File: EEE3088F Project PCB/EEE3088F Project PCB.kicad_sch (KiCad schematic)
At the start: 53 parts, among them IC1 74LVC1G04SE-7, J1 JST PH 2.00mm connector, J3 TYPE-C-31-M-12, J4 TYPE-C-31-M-12, SW1 SS12D07VG5 087, U1 DRV8833PWR, U10 LM7805_TO220, U11 TC4056A., U2 DRV8833PWPR, U3 INA219AxD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

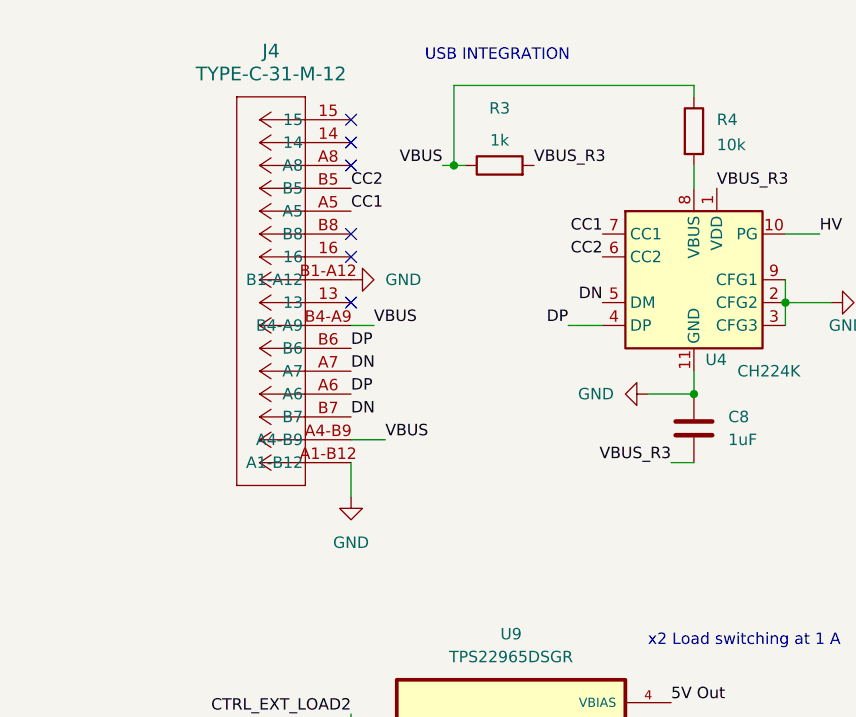
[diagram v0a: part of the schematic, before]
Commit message: Added student numbers, corrected board boundries, placed connectors (USB, JST, & pin headers)
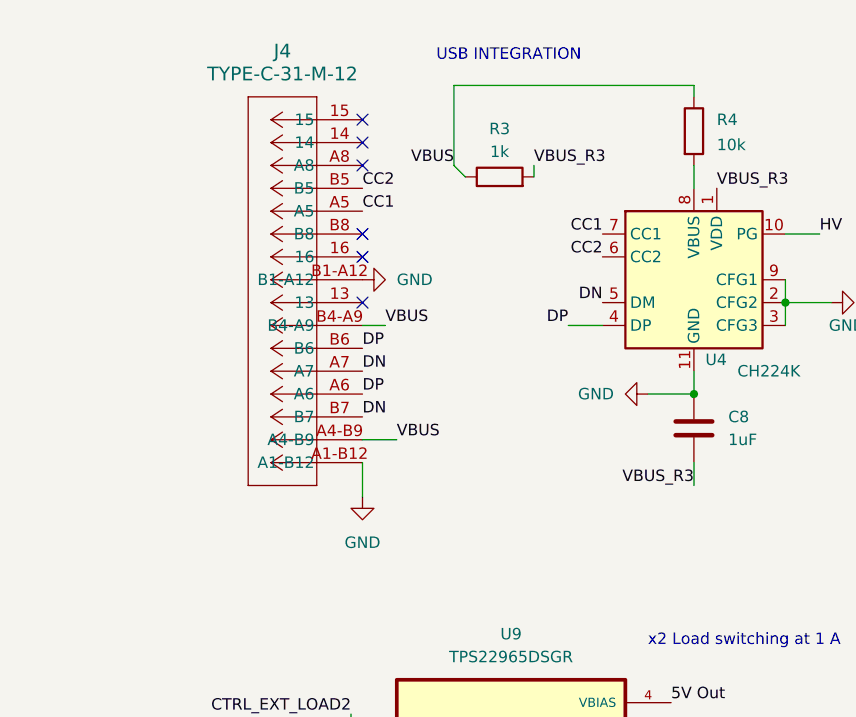
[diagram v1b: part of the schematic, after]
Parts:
- J3, J4: footprint CONN12_C-31-M-12_HRO -> (none)
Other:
- moved on the sheet: J4, R3
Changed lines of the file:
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@@
 	(text "USB INTEGRATION"
 		(exclude_from_sim no)
-		(at 48.006 15.748 0)
+		(at 49.276 15.748 0)
 		(effects
 			(font
@@
 	)
 	(junction
-		(at 43.18 27.94)
-		(diameter 0)
-		(color 0 0 0 0)
-	)
-	(junction
 		(at 257.81 120.65)
 		(diameter 0)
@@
 	)
 	(no_connect
-		(at 31.75 43.18)
+		(at 33.02 43.18)
 	)
 	(no_connect
-		(at 31.75 22.86)
+		(at 33.02 22.86)
 	)
 	(no_connect
-		(at 31.75 35.56)
+		(at 33.02 35.56)
 	)
 	(no_connect
@@
 	)
 	(no_connect
-		(at 31.75 38.1)
+		(at 33.02 38.1)
 	)
 	(no_connect
@@
 	)
 	(no_connect
-		(at 31.75 25.4)
+		(at 33.02 25.4)
 	)
 	(no_connect
@@
 	)
 	(no_connect
-		(at 31.75 27.94)
+		(at 33.02 27.94)
 	)
 	(wire
@@
 	(wire
 		(pts
-			(xy 41.91 27.94) (xy 43.18 27.94)
-		)
-		(stroke
-			(width 0)
-			(type default)
-		)
-	)
-	(wire
-		(pts
 			(xy 110.49 20.32) (xy 110.49 21.59)
 		)
@@
 	(wire
 		(pts
-			(xy 67.31 60.96) (xy 69.85 60.96)
+			(xy 69.85 63.5) (xy 69.85 60.96)
 		)
 		(stroke
@@
 	(wire
 		(pts
+			(xy 44.45 29.21) (xy 43.18 27.94)
+		)
+		(stroke
+			(width 0)
+			(type default)
+		)
+	)
+	(wire
+		(pts
 			(xy 91.44 128.27) (xy 86.36 128.27)
 		)
@@
 	(wire
 		(pts
-			(xy 35.56 58.42) (xy 31.75 58.42)
+			(xy 36.83 58.42) (xy 33.02 58.42)
 		)
 		(stroke
@@
 	(wire
 		(pts
-			(xy 43.18 27.94) (xy 44.45 27.94)
-		)
-		(stroke
-			(width 0)
-			(type default)
-		)
-	)
-	(wire
-		(pts
 			(xy 17.78 181.61) (xy 17.78 172.72)
 		)
@@
 	(wire
 		(pts
-			(xy 34.29 45.72) (xy 31.75 45.72)
+			(xy 35.56 45.72) (xy 33.02 45.72)
 		)
 		(stroke
@@
 	(wire
 		(pts
-			(xy 31.75 64.77) (xy 31.75 60.96)
+			(xy 33.02 64.77) (xy 33.02 60.96)
 		)
 		(stroke
@@
 	(wire
 		(pts
+			(xy 52.07 29.21) (xy 52.07 27.94)
+		)
+		(stroke
+			(width 0)
+			(type default)
+		)
+	)
+	(wire
+		(pts
 			(xy 176.53 123.19) (xy 185.42 123.19)
 		)
@@
 	)
 	(label "DP"
-		(at 31.75 48.26 0)
+		(at 33.02 48.26 0)
 		(effects
 			(font
@@
 	)
 	(label "VBUS"
-		(at 34.29 45.72 0)
+		(at 35.56 45.72 0)
 		(effects
 			(font
@@
 	)
 	(label "VBUS"
-		(at 35.56 58.42 0)
+		(at 36.83 58.42 0)
 		(effects
 			(font
@@
 	)
 	(label "CC1"
-		(at 31.75 33.02 0)
+		(at 33.02 33.02 0)
 		(effects
 			(font
@@
 	)
 	(label "DN"
-		(at 31.75 55.88 0)
+		(at 33.02 55.88 0)
 		(effects
 			(font
@@
 	)
 	(label "CC2"
-		(at 31.75 30.48 0)
+		(at 33.02 30.48 0)
 		(effects
 			(font
@@
 	)
 	(label "VBUS_R3"
-		(at 67.31 60.96 180)
+		(at 69.85 63.5 180)
 		(effects
 			(font
@@
 	)
 	(label "DN"
-		(at 31.75 50.8 0)
+		(at 33.02 50.8 0)
 		(effects
 			(font
@@
 	)
 	(label "DP"
-		(at 31.75 53.34 0)
+		(at 33.02 53.34 0)
 		(effects
 			(font
@@
 	)
 	(label "VBUS"
-		(at 41.91 27.94 180)
+		(at 43.18 27.94 180)
 		(effects
 			(font
@@
 		(polyline
 			(pts
-				(xy 228.6 114.3) (xy 157.48 114.3) (xy 157.48 166.37) (xy 285.75 165.1) (xy 285.75 129.54) (xy 228.6 129.54)
+				(xy 219.71 12.7) (xy 219.71 78.74) (xy 284.48 78.74) (xy 284.48 12.7)
 			)
 			(stroke
@@
 		(polyline
 			(pts
-				(xy 91.44 12.7) (xy 91.44 78.74) (xy 219.71 78.74) (xy 219.71 12.7)
+				(xy 228.6 78.74) (xy 228.6 129.54) (xy 284.48 129.54) (xy 284.48 81.28) (xy 281.94 78.74)
 			)
 			(stroke
@@
 		(polyline
 			(pts
-				(xy 219.71 12.7) (xy 219.71 78.74) (xy 284.48 78.74) (xy 284.48 12.7)
+				(xy 12.7 78.74) (xy 11.43 153.67) (xy 110.49 153.67) (xy 110.49 78.74)
 			)
 			(stroke
@@
 		(polyline
 			(pts
-				(xy 228.6 78.74) (xy 228.6 129.54) (xy 284.48 129.54) (xy 284.48 81.28) (xy 281.94 78.74)
+				(xy 91.44 12.7) (xy 91.44 78.74) (xy 219.71 78.74) (xy 219.71 12.7)
 			)
 			(stroke
@@
 		(polyline
 			(pts
-				(xy 12.7 78.74) (xy 11.43 153.67) (xy 110.49 153.67) (xy 110.49 78.74)
+				(xy 228.6 114.3) (xy 157.48 114.3) (xy 157.48 166.37) (xy 285.75 165.1) (xy 285.75 129.54) (xy 228.6 129.54)
 			)
 			(stroke
@@
 			)
 		)
-		(property "Footprint" "CONN12_C-31-M-12_HRO"
+		(property "Footprint" ""
 			(at -5472.43 10839.45 0)
 			(effects
@@
 	(symbol
 		(lib_id "power:GND")
-		(at 31.75 64.77 0)
+		(at 33.02 64.77 0)
 		(unit 1)
 		(exclude_from_sim no)
@@
 		(fields_autoplaced yes)
 		(property "Reference" "#PWR016"
-			(at 31.75 71.12 0)
+			(at 33.02 71.12 0)
 			(effects
 				(font
@@
 		)
 		(property "Value" "GND"
-			(at 31.75 69.85 0)
+			(at 33.02 69.85 0)
 			(effects
 				(font
@@
 		)
 		(property "Footprint" ""
-			(at 31.75 64.77 0)
+			(at 33.02 64.77 0)
 			(effects
 				(font
@@
 		)
 		(property "Datasheet" ""
-			(at 31.75 64.77 0)
+			(at 33.02 64.77 0)
 			(effects
 				(font
@@
 		)
 		(property "Description" "Power symbol creates a global label with name \"GND\" , ground"
-			(at 31.75 64.77 0)
+			(at 33.02 64.77 0)
 			(effects
 				(font
@@
 	(symbol
 		(lib_id "power:GND")
-		(at 31.75 40.64 90)
+		(at 33.02 40.64 90)
 		(unit 1)
 		(exclude_from_sim no)
@@
 		(fields_autoplaced yes)
 		(property "Reference" "#PWR041"
-			(at 38.1 40.64 0)
+			(at 39.37 40.64 0)
 			(effects
 				(font
@@
 		)
 		(property "Value" "GND"
-			(at 35.56 40.6399 90)
+			(at 36.83 40.6399 90)
 			(effects
 				(font
@@
 		)
 		(property "Footprint" ""
-			(at 31.75 40.64 0)
+			(at 33.02 40.64 0)
 			(effects
 				(font
@@
 		)
 		(property "Datasheet" ""
-			(at 31.75 40.64 0)
+			(at 33.02 40.64 0)
 			(effects
 				(font
@@
 		)
 		(property "Description" "Power symbol creates a global label with name \"GND\" , ground"
-			(at 31.75 40.64 0)
+			(at 33.02 40.64 0)
 			(effects
 				(font
@@
 	(symbol
 		(lib_id "USBC_power_PCB:TYPE-C-31-M-12")
-		(at 31.75 60.96 180)
+		(at 33.02 60.96 180)
 		(unit 1)
 		(exclude_from_sim no)
@@
 		(fields_autoplaced yes)
 		(property "Reference" "J4"
-			(at 22.86 15.24 0)
+			(at 24.13 15.24 0)
 			(effects
 				(font
@@
 		)
 		(property "Value" "TYPE-C-31-M-12"
-			(at 22.86 17.78 0)
+			(at 24.13 17.78 0)
 			(effects
 				(font
@@
 			)
 		)
-		(property "Footprint" "CONN12_C-31-M-12_HRO"
-			(at 31.75 60.96 0)
+		(property "Footprint" ""
+			(at 33.02 60.96 0)
 			(effects
 				(font
@@
 		)
 		(property "Datasheet" "TYPE-C-31-M-12"
-			(at 31.75 60.96 0)
+			(at 33.02 60.96 0)
 			(effects
 				(font
@@
 		)
 		(property "Description" ""
-			(at 31.75 60.96 0)
+			(at 33.02 60.96 0)
 			(effects
 				(font
@@
 	(symbol
 		(lib_id "Device:R")
-		(at 48.26 27.94 90)
+		(at 48.26 29.21 90)
 		(unit 1)
 		(exclude_from_sim no)
@@
 		(dnp no)
 		(property "Reference" "R3"
-			(at 48.26 21.59 90)
+			(at 48.26 23.876 90)
 			(effects
 				(font
@@
 		)
 		(property "Value" "1k"
-			(at 48.26 25.146 90)
+			(at 48.26 26.416 90)
 			(effects
 				(font
@@
 		)
 		(property "Footprint" "exported_footprints:RESC3115X65N"
-			(at 48.26 29.718 90)
+			(at 48.26 30.988 90)
 			(effects
 				(font
@@
 		)
 		(property "Datasheet" "~"
-			(at 48.26 27.94 0)
+			(at 48.26 29.21 0)
 			(effects
 				(font
@@
 		)
 		(property "Description" "Resistor"
-			(at 48.26 27.94 0)
+			(at 48.26 29.21 0)
 			(effects
 				(font

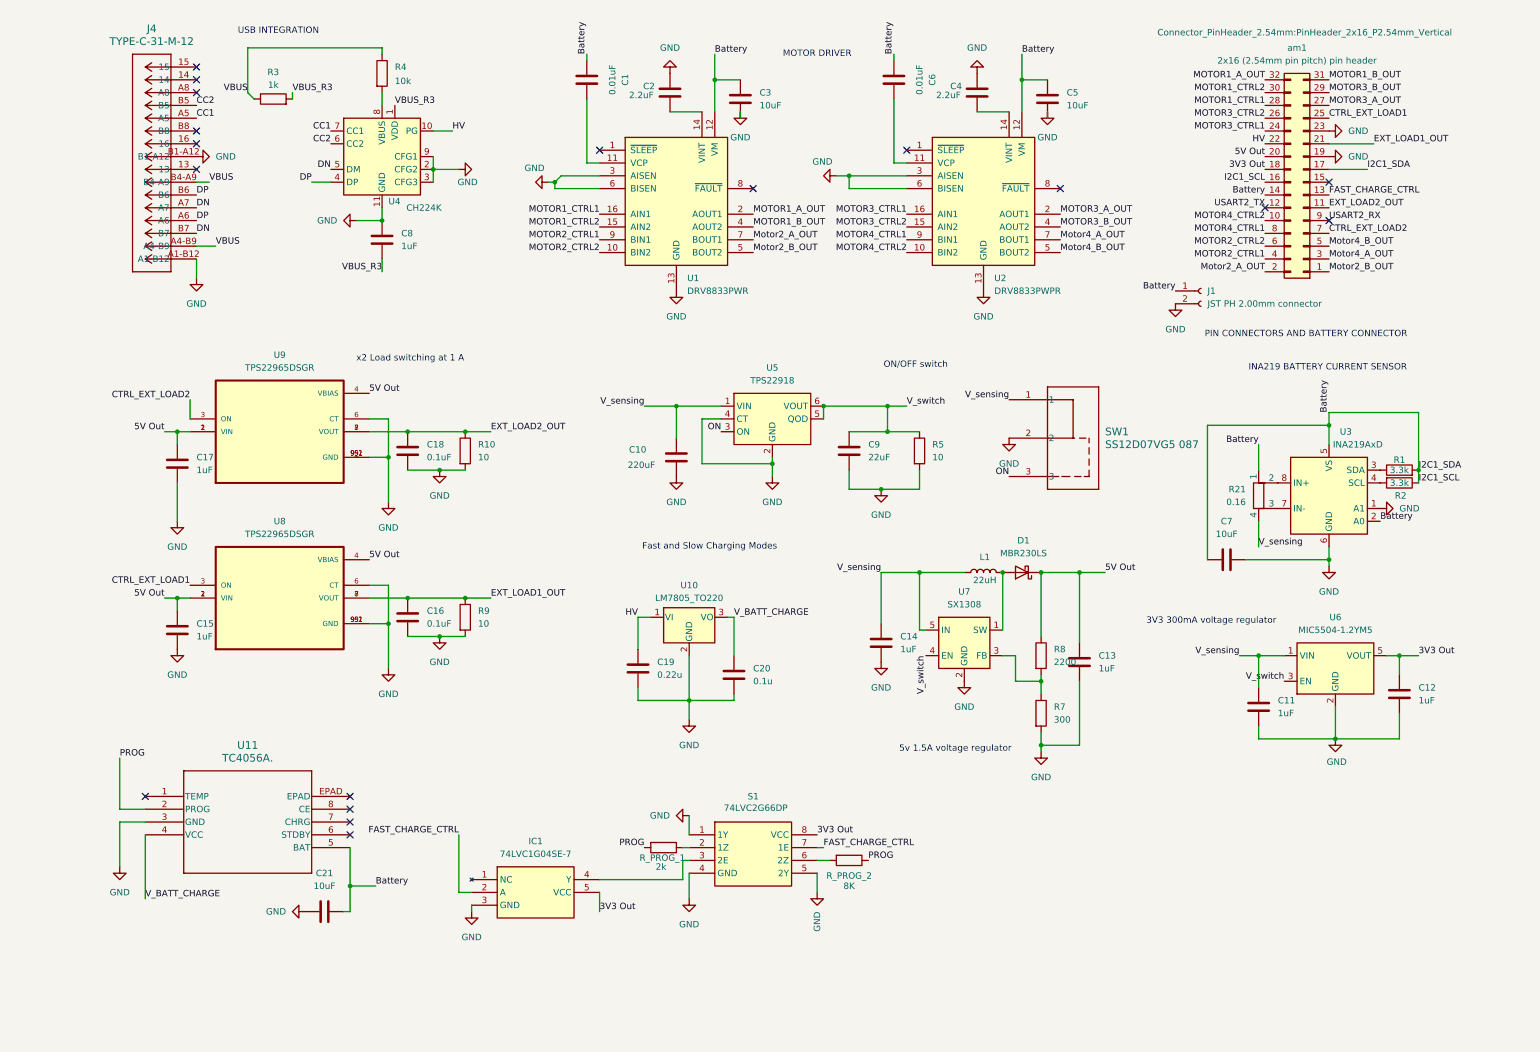
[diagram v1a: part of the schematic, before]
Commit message: added fault managment and testing points for USB Integration and Charging requirments
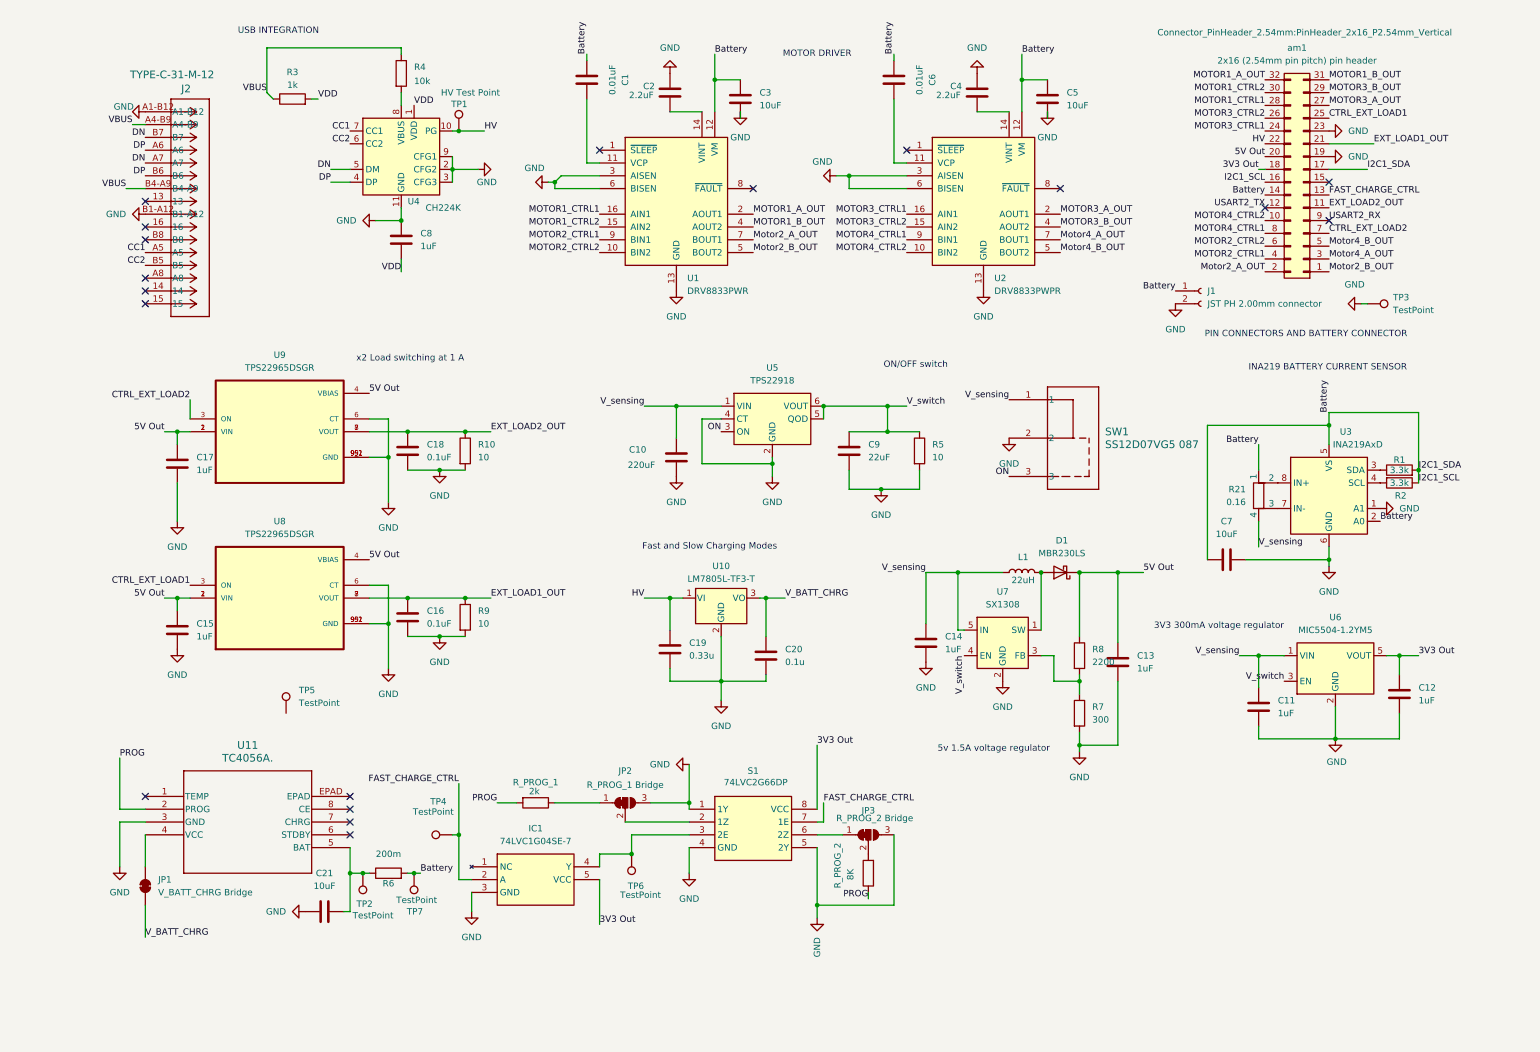
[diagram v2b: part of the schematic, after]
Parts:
- removed J4: TYPE-C-31-M-12, symbol USBC_power_PCB:TYPE-C-31-M-12
- added J2: TYPE-C-31-M-12, CONN12_C-31-M-12_HRO, symbol TYPE-C:TYPE-C-31-M-12
- added JP1: V_BATT_CHRG Bridge, Jumper:SolderJumper-2_P1.3mm_Bridged2Bar_Pad1.0x1.5mm, symbol Jumper:SolderJumper_2_Bridged
- added JP2: R_PROG_1 Bridge, symbol Jumper:SolderJumper_3_Bridged12
- added JP3: R_PROG_2 Bridge, Jumper:SolderJumper-3_P1.3mm_Bridged2Bar12_Pad1.0x1.5mm_NumberLabels, symbol Jumper:SolderJumper_3_Bridged12
- added R6: 200m, Resistor_SMD:R_Shunt_Vishay_WSR2_WSR3, symbol Device:R
- added TP1: HV Test Point, TestPoint:TestPoint_Pad_1.0x1.0mm, symbol Connector:TestPoint
- added TP2, TP4, TP7: TestPoint, TestPoint:TestPoint_Pad_1.0x1.0mm, symbol Connector:TestPoint
- added TP3: TestPoint, TestPoint:TestPoint_Pad_2.0x2.0mm, symbol Connector:TestPoint
- added TP5, TP6: TestPoint, symbol Connector:TestPoint
- C19: value 0.22u -> 0.33u
- U10: value LM7805_TO220 -> LM7805L-TF3-T
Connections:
- net Battery: now also R6.2, TP7.1; no longer C21.2, U11.5 (BAT)
- net CC1: now also J2.A5
- net CC2: now also J2.B5
- net DN: now also J2.A7, J2.B7
- net DP: now also J2.A6, J2.B6
- net FAST_CHARGE_CTRL: now also TP4.1
- net GND: now also J2.A1-B12, J2.B1-A12, JP2.3 (B), JP3.3 (B), TP3.1
- net HV: now also TP1.1
- net VBUS: now also J2.A4-B9, J2.B4-A9
- net at S1.2 (1Z): now also JP2.2 (C); no longer R_PROG_1.1
- net at IC1.4 (Y), S1.3 (2E): now also TP6.1
- net at S1.6 (2Z): now also JP3.1 (A); no longer R_PROG_2.2
- net VBUS_R3 renamed VDD
- net V_BATT_CHARGE renamed V_BATT_CHRG
- net V_BATT_CHRG: now also JP1.1 (A); no longer U11.4 (VCC)
- new net: C21.2, R6.1, TP2.1, U11.5 (BAT)
- new net: JP3.2 (C), R_PROG_2.2
- new net: JP2.1 (A), R_PROG_1.1
- new net: JP1.2 (B), U11.4 (VCC)
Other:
- moved on the sheet: C13, C14, C19, C20, C8, D1, IC1, L1, R3, R4, R7, R8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
